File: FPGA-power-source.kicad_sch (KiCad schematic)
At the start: 13 parts, among them U1 TPS54325PWPR

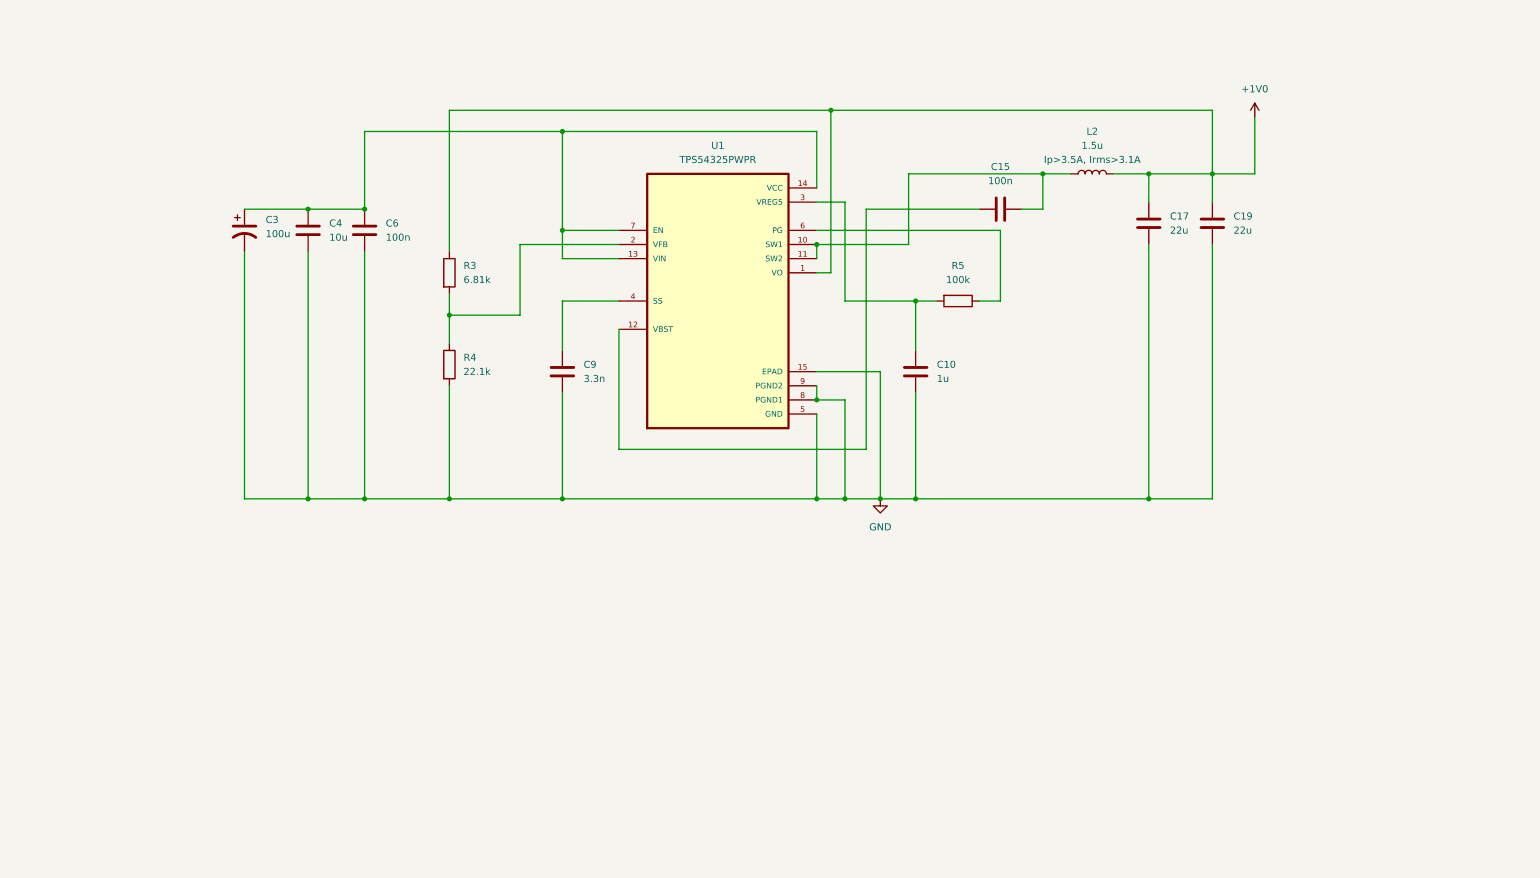
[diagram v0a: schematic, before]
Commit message: FPGA power source passes ERC
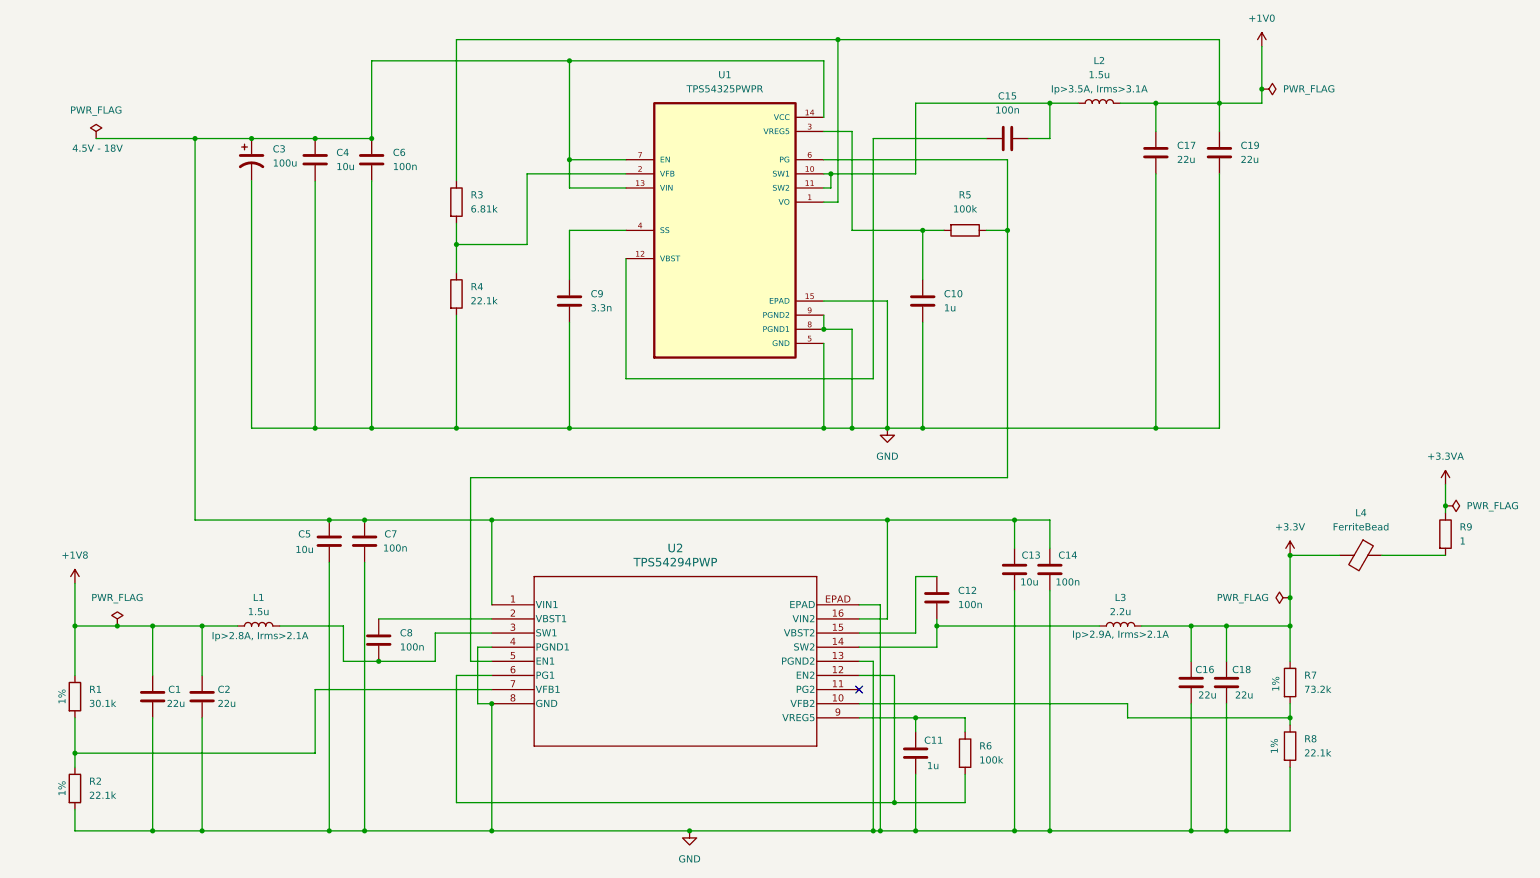
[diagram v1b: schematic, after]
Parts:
- added C1, C2: 22u, Capacitor_SMD:C_0805_2012Metric, symbol Device:C
- added C11: 1u, symbol Device:C
- added C12, C14, C7, C8: 100n, symbol Device:C
- added C13: 10u, symbol Device:C
- added C16, C18: 22u, symbol Device:C
- added C5: 10u, Capacitor_SMD:C_0805_2012Metric, symbol Device:C
- added L1: 1.5u, Inductor_SMD:L_0805_2012Metric, symbol Device:L
- added L3: 2.2u, Inductor_SMD:L_0805_2012Metric, symbol Device:L
- added L4: FerriteBead, symbol Device:FerriteBead
- added R1: 30.1k, symbol Device:R
- added R2, R8: 22.1k, symbol Device:R
- added R6: 100k, symbol Device:R
- added R7: 73.2k, symbol Device:R
- added R9: 1, symbol Device:R
- added U2: TPS54294PWP, TPS54294PWP:PWP16_2P31X2P46, symbol TPS54294:TPS54294PWP
- C3, C4: footprint (none) -> Capacitor_SMD:C_0805_2012Metric
- L2: footprint (none) -> Inductor_SMD:L_0805_2012Metric
- U1: footprint TPS54325PWPR:IC_TPS27S100BPWPR -> TPS54325PWPR:PWP14_2P31X2P46
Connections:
- net GND: now also C1.2, C11.2, C13.2, C14.2, C16.2, C18.2, C2.1, C5.2, C7.2, R2.2, R8.2, U2.13 (PGND2), U2.4 (PGND1), U2.8 (GND), U2.EPAD
- net at R5.1, U1.6 (PG): now also U2.5 (EN1)
- net at C3.1, C4.1, C6.1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: now also C13.1, C14.1, C5.1, C7.1, U2.1 (VIN1), U2.16 (VIN2)
- new net: R7.2, R8.1, U2.10 (VFB2)
- new net: C8.2, L1.2, U2.3 (SW1)
- new net: C12.2, L3.1, U2.14 (SW2)
- new net: R6.2, U2.12 (EN2), U2.6 (PG1)
- new net: C12.1, U2.15 (VBST2)
- new net: C8.1, U2.2 (VBST1)
- new net: R1.2, R2.1, U2.7 (VFB1)
- new net: C11.1, R6.1, U2.9 (VREG5)
- new net: L4.1, R9.2
- new net +1V8: C1.1, C2.2, L1.1, R1.1
- new net +3.3V: C16.1, C18.1, L3.2, L4.2, R7.1
- new net +3.3VA: R9.1
- no-connect marks 0 -> 1
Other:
- moved on the sheet: C10, C15, C17, C19, C3, C4, C6, C9, L2, R3, R4, R5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

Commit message: layout changes
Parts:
- R1, R2, R3, R4, R5, R6, R7, R8, R9: footprint (none) -> Resistor_SMD:R_0805_2012Metric
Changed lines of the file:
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@@
 	)
 	(junction
+		(at 173.99 52.07)
+		(diameter 0)
+		(color 0 0 0 0)
+	)
+	(junction
 		(at 175.26 160.02)
 		(diameter 0)
@@
 	)
 	(junction
+		(at 161.29 64.77)
+		(diameter 0)
+		(color 0 0 0 0)
+	)
+	(junction
 		(at 76.2 160.02)
 		(diameter 0)
@@
 	(wire
 		(pts
-			(xy 163.83 52.07) (xy 176.53 52.07)
+			(xy 163.83 52.07) (xy 173.99 52.07)
 		)
 		(stroke
@@
 	(wire
 		(pts
+			(xy 173.99 52.07) (xy 176.53 52.07)
+		)
+		(stroke
+			(width 0)
+			(type default)
+		)
+	)
+	(wire
+		(pts
 			(xy 77.47 21.59) (xy 77.47 35.56)
 		)
@@
 	(wire
 		(pts
+			(xy 161.29 64.77) (xy 170.18 64.77)
+		)
+		(stroke
+			(width 0)
+			(type default)
+		)
+	)
+	(wire
+		(pts
 			(xy 123.19 41.91) (xy 105.41 41.91)
 		)
@@
 	(wire
 		(pts
-			(xy 158.75 64.77) (xy 170.18 64.77)
+			(xy 158.75 64.77) (xy 161.29 64.77)
 		)
 		(stroke
@@
 			)
 		)
-		(property "Footprint" ""
+		(property "Footprint" "Resistor_SMD:R_0805_2012Metric"
 			(at 240.792 133.35 90)
 			(effects
@@
 			)
 		)
-		(property "Footprint" ""
+		(property "Footprint" "Resistor_SMD:R_0805_2012Metric"
 			(at 184.15 50.292 90)
 			(effects
@@
 			)
 		)
-		(property "Footprint" ""
+		(property "Footprint" "Resistor_SMD:R_0805_2012Metric"
 			(at 240.792 144.78 90)
 			(effects
@@
 			)
 		)
-		(property "Footprint" ""
+		(property "Footprint" "Resistor_SMD:R_0805_2012Metric"
 			(at 22.352 152.4 90)
 			(effects
@@
 	(symbol
 		(lib_id "power:PWR_FLAG")
+		(at 173.99 52.07 0)
+		(unit 1)
+		(exclude_from_sim no)
+		(in_bom yes)
+		(on_board yes)
+		(dnp no)
+		(fields_autoplaced yes)
+		(property "Reference" "#FLG06"
+			(at 173.99 50.165 0)
+			(effects
+				(font
+					(size 1.27 1.27)
+				)
+				(hide yes)
+			)
+		)
+		(property "Value" "PWR_FLAG"
+			(at 173.99 46.99 0)
+			(effects
+				(font
+					(size 1.27 1.27)
+				)
+			)
+		)
+		(property "Footprint" ""
+			(at 173.99 52.07 0)
+			(effects
+				(font
+					(size 1.27 1.27)
+				)
+				(hide yes)
+			)
+		)
+		(property "Datasheet" "~"
+			(at 173.99 52.07 0)
+			(effects
+				(font
+					(size 1.27 1.27)
+				)
+				(hide yes)
+			)
+		)
+		(property "Description" "Special symbol for telling ERC where power comes from"
+			(at 173.99 52.07 0)
+			(effects
+				(font
+					(size 1.27 1.27)
+				)
+				(hide yes)
+			)
+		)
+		(pin "1"
+		)
+		(instances
+			(project ""
+				(path "/071102f3-276b-4b6b-8738-8c534a30b197/f7dbf63d-f891-4c8e-a7a2-66a57df960da"
+					(reference "#FLG06")
+					(unit 1)
+				)
+			)
+		)
+	)
+	(symbol
+		(lib_id "power:PWR_FLAG")
 		(at 242.57 118.11 90)
 		(unit 1)
@@
 			)
 		)
-		(property "Footprint" ""
+		(property "Footprint" "Resistor_SMD:R_0805_2012Metric"
 			(at 22.352 135.89 90)
 			(effects
@@
 			)
 		)
-		(property "Footprint" ""
+		(property "Footprint" "Resistor_SMD:R_0805_2012Metric"
 			(at 90.932 46.99 90)
 			(effects
@@
 			)
 		)
-		(property "Footprint" ""
+		(property "Footprint" "Resistor_SMD:R_0805_2012Metric"
 			(at 90.932 63.5 90)
 			(effects
@@
 			)
 		)
-		(property "Footprint" ""
+		(property "Footprint" "Resistor_SMD:R_0805_2012Metric"
 			(at 268.732 106.68 90)
 			(effects
@@
 	)
 	(symbol
+		(lib_id "power:PWR_FLAG")
+		(at 161.29 64.77 0)
+		(unit 1)
+		(exclude_from_sim no)
+		(in_bom yes)
+		(on_board yes)
+		(dnp no)
+		(fields_autoplaced yes)
+		(property "Reference" "#FLG07"
+			(at 161.29 62.865 0)
+			(effects
+				(font
+					(size 1.27 1.27)
+				)
+				(hide yes)
+			)
+		)
+		(property "Value" "PWR_FLAG"
+			(at 161.29 59.69 0)
+			(effects
+				(font
+					(size 1.27 1.27)
+				)
+			)
+		)
+		(property "Footprint" ""
+			(at 161.29 64.77 0)
+			(effects
+				(font
+					(size 1.27 1.27)
+				)
+				(hide yes)
+			)
+		)
+		(property "Datasheet" "~"
+			(at 161.29 64.77 0)
+			(effects
+				(font
+					(size 1.27 1.27)
+				)
+				(hide yes)
+			)
+		)
+		(property "Description" "Special symbol for telling ERC where power comes from"
+			(at 161.29 64.77 0)
+			(effects
+				(font
+					(size 1.27 1.27)
+				)
+				(hide yes)
+			)
+		)
+		(pin "1"
+		)
+		(instances
+			(project ""
+				(path "/071102f3-276b-4b6b-8738-8c534a30b197/f7dbf63d-f891-4c8e-a7a2-66a57df960da"
+					(reference "#FLG07")
+					(unit 1)
+				)
+			)
+		)
+	)
+	(symbol
 		(lib_id "Device:C")
 		(at 193.04 113.03 0)
@@
 			)
 		)
-		(property "Footprint" ""
+		(property "Footprint" "Resistor_SMD:R_0805_2012Metric"
 			(at 182.372 146.05 90)
 			(effects
